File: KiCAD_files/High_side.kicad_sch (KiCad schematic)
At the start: 27 parts

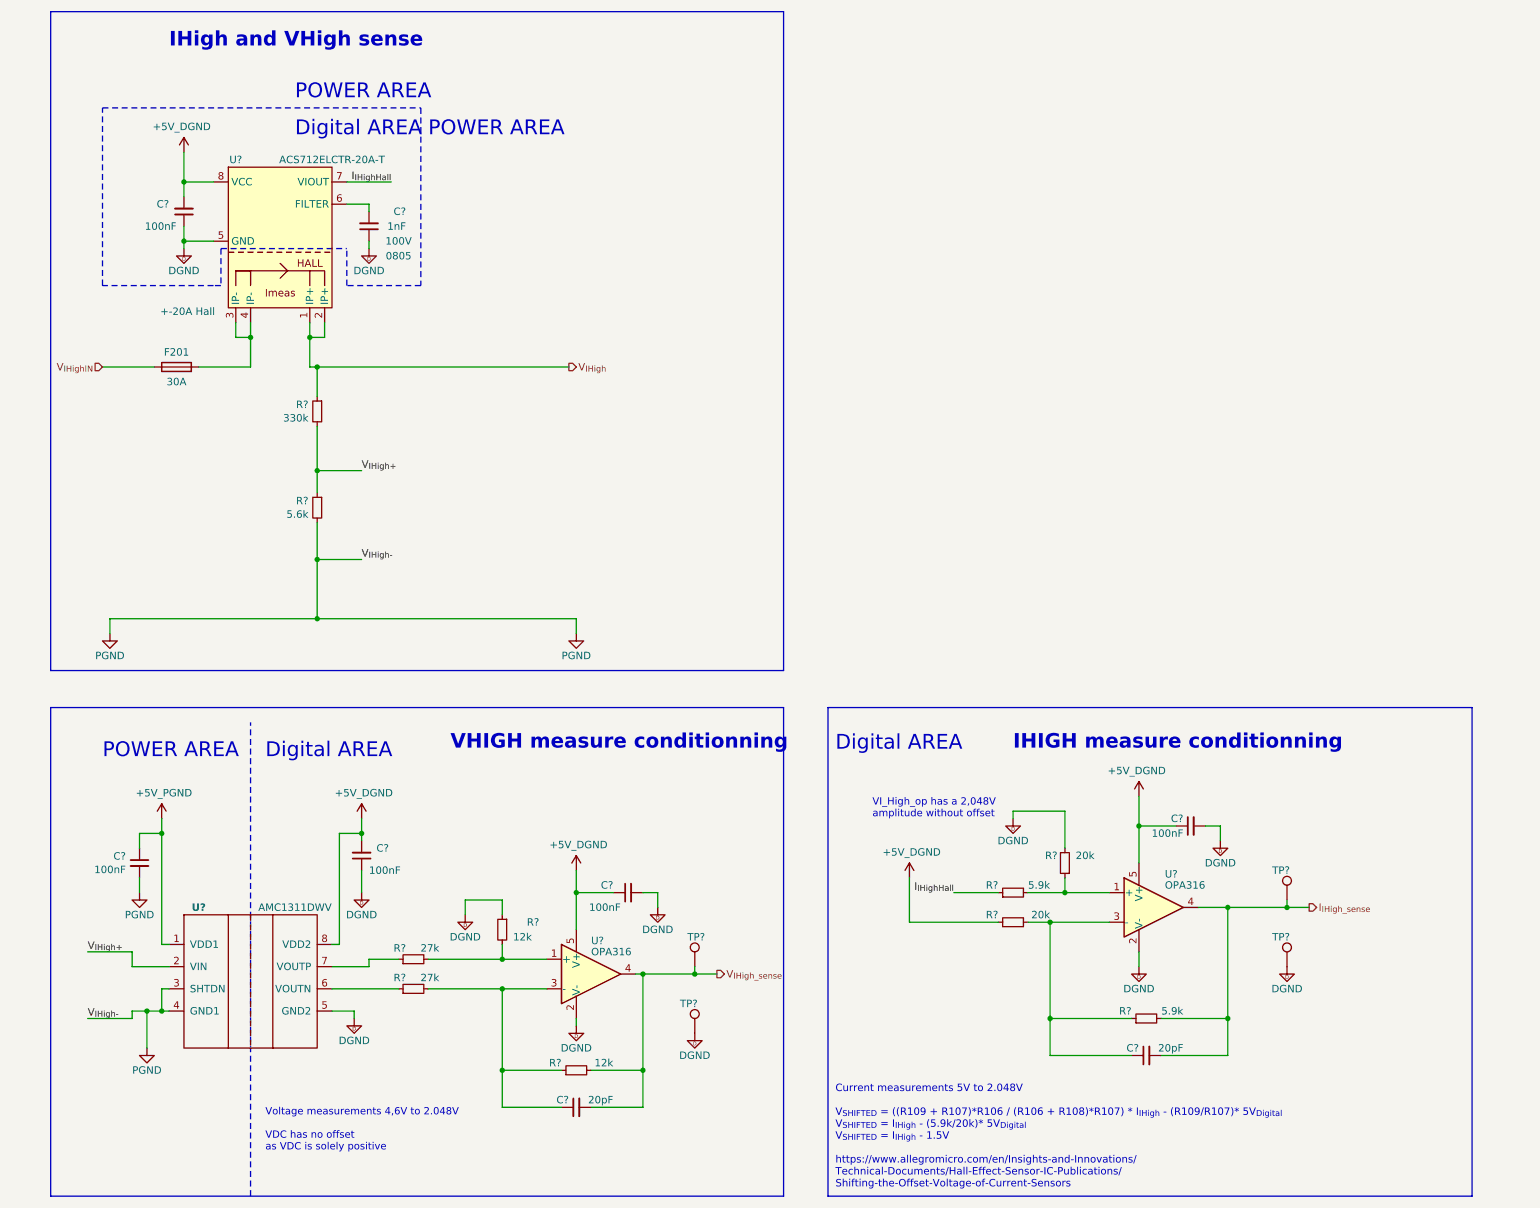
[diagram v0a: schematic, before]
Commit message: Added ERC rules for galvanic isolation. Modified SPIN pinout.
Signed-off-by: Jean Alinei <jean.alinei@laas.fr>
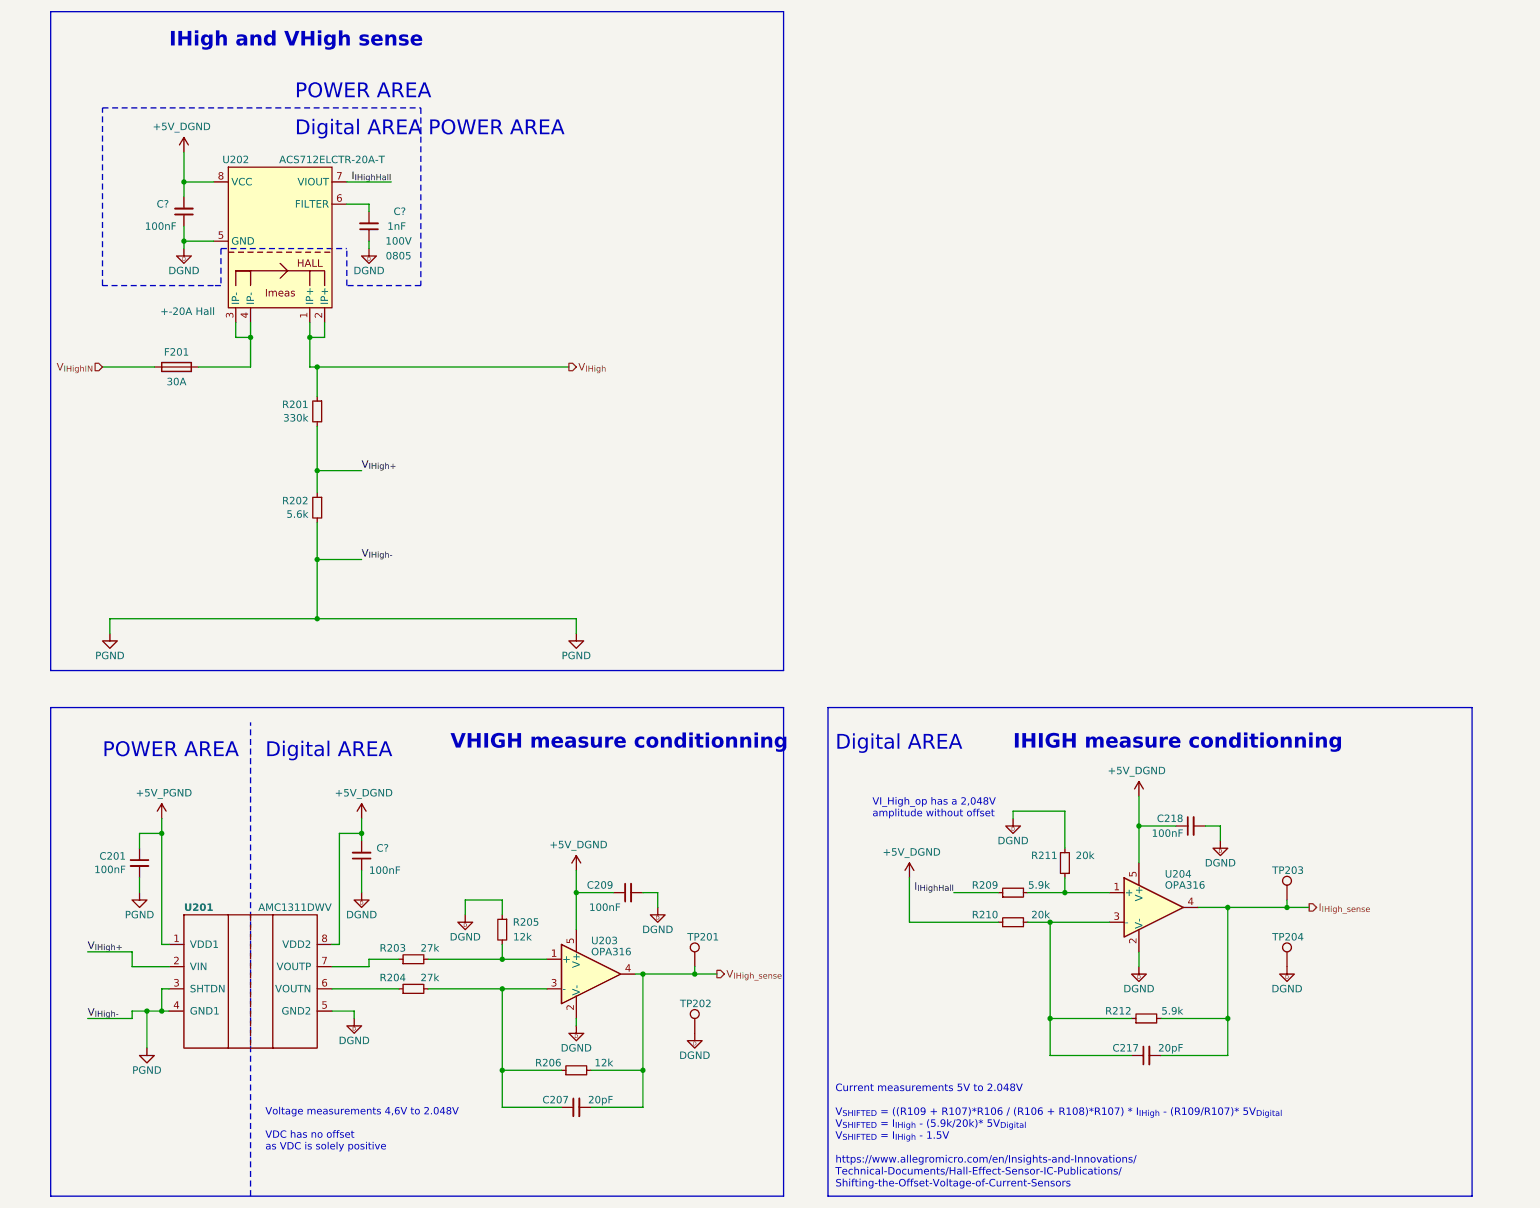
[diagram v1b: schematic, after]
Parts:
- gave numbers to parts that had none: 23
